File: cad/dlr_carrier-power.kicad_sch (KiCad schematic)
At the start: 25 parts, among them J1 PV_IN, J2 BQ24650, J4 LMR33630ADDA, U1 AP2112K-3.3, U2 LP5907MFX-3.8

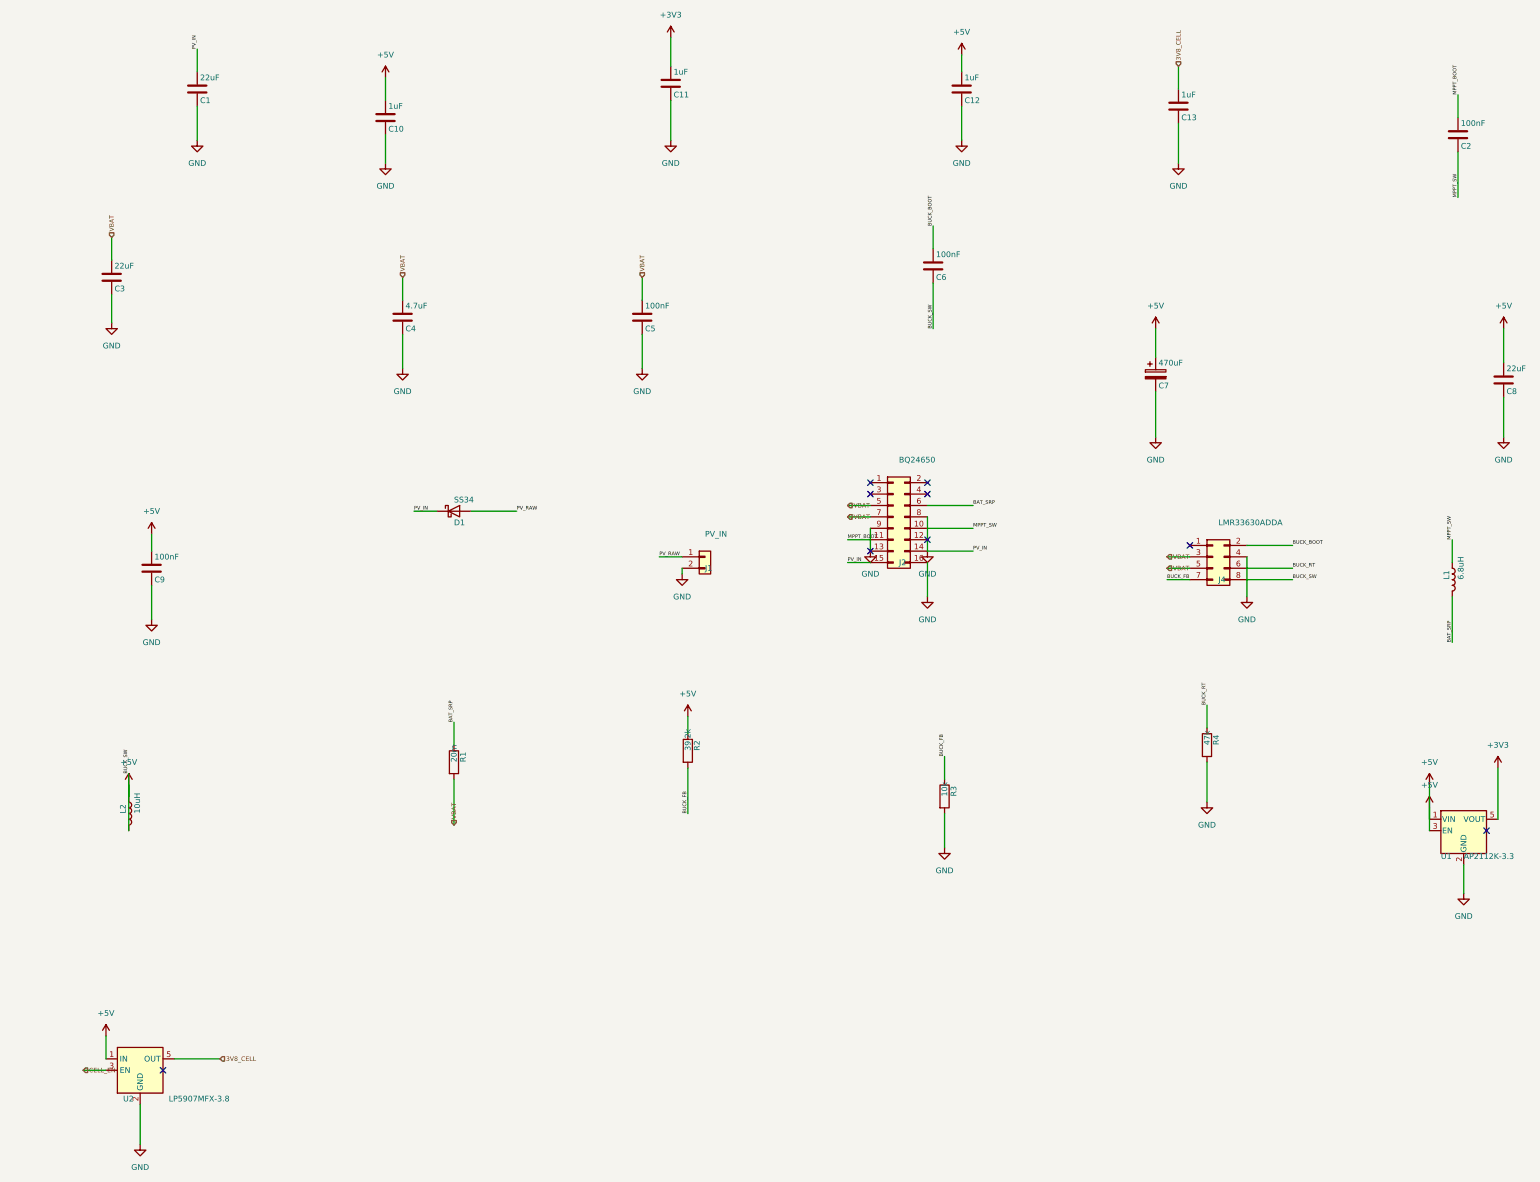
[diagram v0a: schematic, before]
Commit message: 🗺 feat(cad): scripted schematic + board pipeline, 4-layer stack
The committed board had almost every pad on +3V3 — no 5V_RAIL, VBAT or SDA1 net
existed on it at all — so the gerbers in output/ were never a valid board. Cause:
"Update PCB from Schematic" is GUI-only, so nothing kept the board honest, and the
schematic generator itself was merging nets.

Schematic generator:
  * power stubs now run along the pin direction; they used to be forced up or down
    regardless, which drove a 5V_RAIL stub straight through the buck inductor's
    BUCK_SW pin
  * PWR_FLAGs are placed by rule — any net that reaches a power-input pin with no
    power-output pin gets exactly one — instead of a hardcoded list, which is what
    the new VBAT and CHG_VCC rails needed
  * placement is deterministic; it used Python's salted hash(), so no two runs
    produced the same schematic
  * sch_guard fails the build on any cross-net wire/pin collision
  * ~700 lines of dead single-sheet generator removed
  ERC: 0 violations across all 8 sheets.

Board pipeline (cad/drawing/, all scripted, no GUI step):
  sync_pcb      rebuilds every footprint from the library and reassigns every pad
                net from the SKiDL netlist — the replacement for F8
  board_setup   4-layer SIG/GND/5V/SIG stack, rules, net classes, planes (ADR-016)
  route_pcb     DSN -> Freerouting -> SES, after patching the DSN so plane layers
                are "power" (the router was slicing the planes with signals) and
                the plane declarations are dropped (the router had been leaving
                GND and 5V pads with no path to the plane at all)
  stitch_planes vias from surface pads into their plane
  close_gaps    closes what the router leaves, using real segment-to-segment
                clearance; it never forces copper through another net

DRC: 265 unconnected -> 5, with no clearance, short, annular-ring or courtyard
errors. The remaining 5 are escapes on the DF40, the VQFN and the MSOP; they are
l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
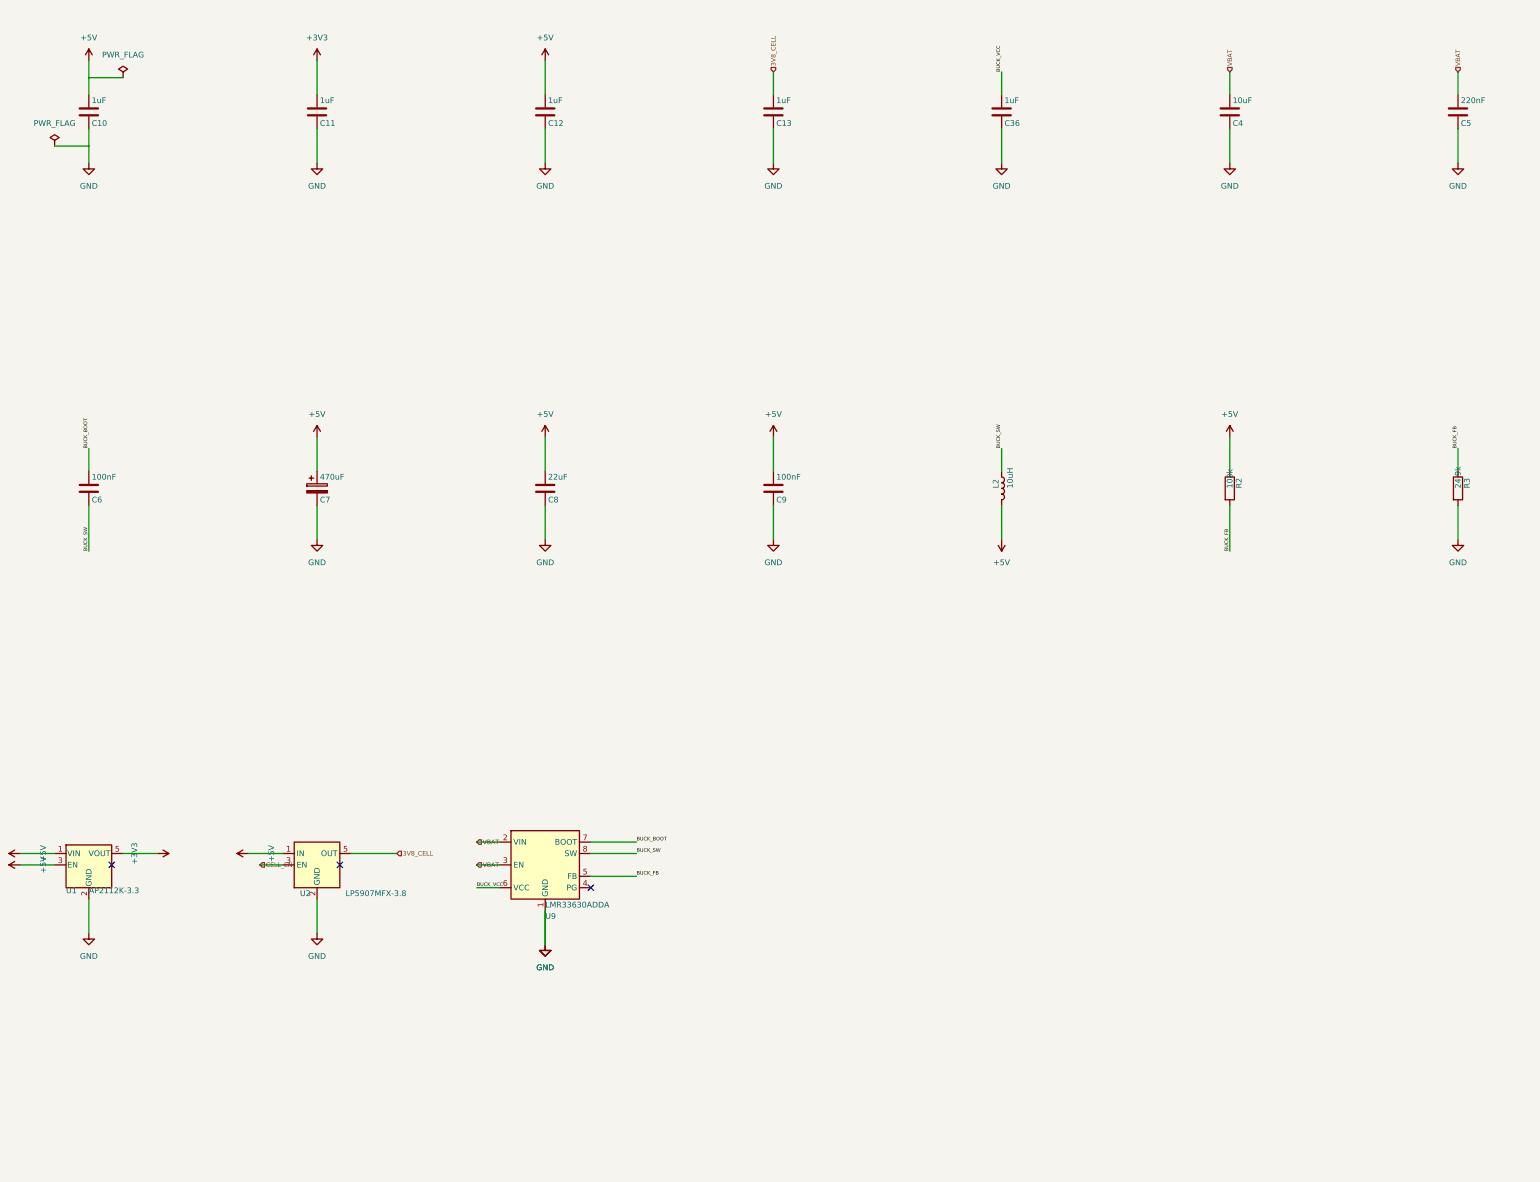
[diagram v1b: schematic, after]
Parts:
- removed C1, C3: 22uF, Capacitor_SMD:C_1206_3216Metric, symbol Device:C
- removed C2: 100nF, Capacitor_SMD:C_0402_1005Metric, symbol Device:C
- removed D1: SS34, Diode_SMD:D_SMA, symbol Device:D_Schottky
- removed J1: PV_IN, TerminalBlock_Phoenix:TerminalBlock_Phoenix_MKDS-1,5-2-5.08_1x02_P5.08mm_Horizontal, symbol Connector_Generic:Conn_01x02
- removed J2: BQ24650, Package_DFN_QFN:HVQFN-16-1EP_3x3mm_P0.5mm_EP1.5x1.5mm, symbol Connector_Generic:Conn_02x08_Odd_Even
- removed J4: LMR33630ADDA, Package_SO:HSOP-8-1EP_3.9x4.9mm_P1.27mm_EP2.41x3.1mm, symbol Connector_Generic:Conn_02x04_Odd_Even
- removed L1: 6.8uH, Inductor_SMD:L_Bourns-SRN6028, symbol Device:L
- removed R1: 20m, Resistor_SMD:R_1206_3216Metric, symbol Device:R
- removed R4: 47k, Resistor_SMD:R_0402_1005Metric, symbol Device:R
- added C36: 1uF, Capacitor_SMD:C_0402_1005Metric, symbol Device:C
- added U9: LMR33630ADDA, Package_SO:Texas_HSOP-8-1EP_3.9x4.9mm_P1.27mm_ThermalVias, symbol Regulator_Switching:LMR33630ADDA
- C4: value 4.7uF -> 10uF; footprint Capacitor_SMD:C_0805_2012Metric -> Capacitor_SMD:C_1206_3216Metric
- C5: value 100nF -> 220nF
- L2: footprint Inductor_SMD:L_Bourns-SRN8040_8x8.15mm -> Inductor_SMD:L_Bourns_SRN8040TA
- R2: value 39.2k -> 100k
- R3: value 10k -> 24.9k
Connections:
- net +5V: no longer C6.2, L2.1
- net BUCK_BOOT: now also U9.7 (BOOT)
- net BUCK_FB: now also U9.5 (FB)
- net GND: now also C36.2, U9.1 (GND), U9.9 (GND)
- net VBAT: now also U9.2 (VIN), U9.3 (EN)
- new net BUCK_SW: C6.2, L2.1, U9.8 (SW)
- new net BUCK_VCC: C36.1, U9.6 (VCC)
- no-connect marks 9 -> 3
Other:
- title: DLR Carrier — POWER -> DLR Carrier — POWER RAILS
